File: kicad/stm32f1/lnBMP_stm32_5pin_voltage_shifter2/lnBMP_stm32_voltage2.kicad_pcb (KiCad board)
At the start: 2 copper layers, 52.6 x 33 mm, 1 part, among them J1 Debug port

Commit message: beginning GD32 version
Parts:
- added C16: 100n, Resistor_SMD:R_0603_1608Metric, F.Cu at (167.3, 68.5)
- added C17: 100n, Resistor_SMD:R_0603_1608Metric, F.Cu at (122.3, 104.0)
- added C18: 100n, Resistor_SMD:R_0603_1608Metric, F.Cu at (122.3, 106.5)
- added C19: 100n, Resistor_SMD:R_0603_1608Metric, F.Cu at (122.3, 109.0)
- added C20: 100n, Resistor_SMD:R_0603_1608Metric, F.Cu at (122.3, 111.5)
- added C22: 100n, Resistor_SMD:R_0603_1608Metric, F.Cu at (134.2, 107.3)
- added C24: 100n, Resistor_SMD:R_0603_1608Metric, F.Cu at (134.2, 109.8)
- added C3: 100n, Resistor_SMD:R_0603_1608Metric, F.Cu at (166.0, 74.5)
- added C4: 100n, Resistor_SMD:R_0603_1608Metric, F.Cu at (112.5, 58.2)
- added C5: 100u, Capacitor_SMD:C_1206_3216Metric_Pad1.33x1.80mm_HandSolder, F.Cu at (148.2, 81.0)
- added C6: 100n, Resistor_SMD:R_0603_1608Metric, F.Cu at (148.8, 83.7)
- added C7: 22pf, Resistor_SMD:R_0603_1608Metric, F.Cu at (118.6, 89.8)
- added C8: 22pf, Resistor_SMD:R_0603_1608Metric, F.Cu at (118.6, 93.4)
- added D1: LED, Diode_SMD:D_0805_2012Metric, F.Cu at (143.0, 98.6)
- added D2: LED, Diode_SMD:D_0805_2012Metric, F.Cu at (152.6, 83.3)
- added J2: Debug port, Connector_JST:JST_XH_B5B-XH-AM_1x05_P2.50mm_Vertical, F.Cu at (139.8, 82.5)
- added J3: USB, Connector_USB:USB_C_Receptacle_Palconn_UTC16-G, F.Cu at (150.6, 91.7)
- added J4: DFU, Connector_PinHeader_1.27mm:PinHeader_1x02_P1.27mm_Vertical, F.Cu at (132.2, 57.0)
- added J5: BOOT, Connector_PinHeader_1.27mm:PinHeader_1x02_P1.27mm_Vertical, F.Cu at (136.4, 57.0)
- added J6: jtag, Connector_PinHeader_1.27mm:PinHeader_2x05_P1.27mm_Vertical_SMD, F.Cu at (108.0, 94.3)
- added J9: Conn_01x03_Socket, Connector_PinHeader_1.27mm:PinHeader_1x03_P1.27mm_Vertical, F.Cu at (117.1, 65.4)
- added R1: 10k, Resistor_SMD:R_0603_1608Metric, F.Cu at (141.0, 57.2)
- added R10: 330, Resistor_SMD:R_0603_1608Metric, F.Cu at (152.5, 80.9)
- added R2: 330, Resistor_SMD:R_0603_1608Metric, F.Cu at (142.7, 96.4)
- added R3: 10k, Resistor_SMD:R_0603_1608Metric, F.Cu at (145.0, 58.8)
- added R4: 1k, Resistor_SMD:R_0603_1608Metric, F.Cu at (170.0, 77.0)
- added R5: 22, Resistor_SMD:R_0603_1608Metric, F.Cu at (142.8, 92.7)
- added R6: 22, Resistor_SMD:R_0603_1608Metric, F.Cu at (142.8, 91.1)
- added R7: 1.2k, Resistor_SMD:R_0603_1608Metric, F.Cu at (142.8, 89.5)
- added R8: 5.1k, Resistor_SMD:R_0603_1608Metric, F.Cu at (145.7, 89.0)
- added R9: 5.1k, Resistor_SMD:R_0603_1608Metric, F.Cu at (145.7, 93.9)
- added RST1: SW2, Button_Switch_SMD:SW_SPST_CK_RS282G05A3, F.Cu at (135.6, 52.8)
- added U1: GD32F303, Package_QFP:LQFP-48_7x7mm_P0.5mm, F.Cu at (130.2, 91.4)
- added U2: 3V->VTREF, Package_SO:VSSOP-8_2.3x2mm_P0.5mm, F.Cu at (102.2, 60.5)
- added U3: VTREF->3V, Package_SO:VSSOP-8_2.3x2mm_P0.5mm, F.Cu at (102.1, 49.4)
- added U4: VTREF<->3V, Package_SO:VSSOP-8_2.3x2mm_P0.5mm, F.Cu at (102.1, 55.0)
- added U5: LM1117-3.3, Package_TO_SOT_SMD:SOT-223, F.Cu at (149.3, 74.2)
- added U8: RT9013-33GB, PCM_Package_TO_SOT_SMD_AKL:TSOT-23-5, F.Cu at (102.1, 43.1)
- added Y2: 8Mhz, Crystal:Crystal_SMD_TXC_7M-4Pin_3.2x2.5mm, F.Cu at (121.8, 91.5)
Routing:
- net +3.3V: track 0.00 -> 37.8 mm, vias 0 -> 3
- net GND: track 0.00 -> 37.5 mm
- net Net-(U5-VI): track 0.00 -> 26.4 mm, vias 0 -> 3
- net Net-(U1-PD0): track 0.00 -> 10.4 mm
- net DP: track 0.00 -> 10.1 mm
- net Net-(U1-PD1): track 0.00 -> 9.16 mm
- net Net-(U1-PB13): track 0.00 -> 8.61 mm
- net DN: track 0.00 -> 8.37 mm
- net D-: track 0.00 -> 7.67 mm
- net D+: track 0.00 -> 6.22 mm
- net Net-(J3-CC2): track 0.00 -> 2.42 mm
- net Net-(J3-CC1): track 0.00 -> 2.40 mm
- net Net-(D2-A): track 0.00 -> 1.95 mm
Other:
- board size 52.6 x 33 mm -> 52.6 x 31.7 mm

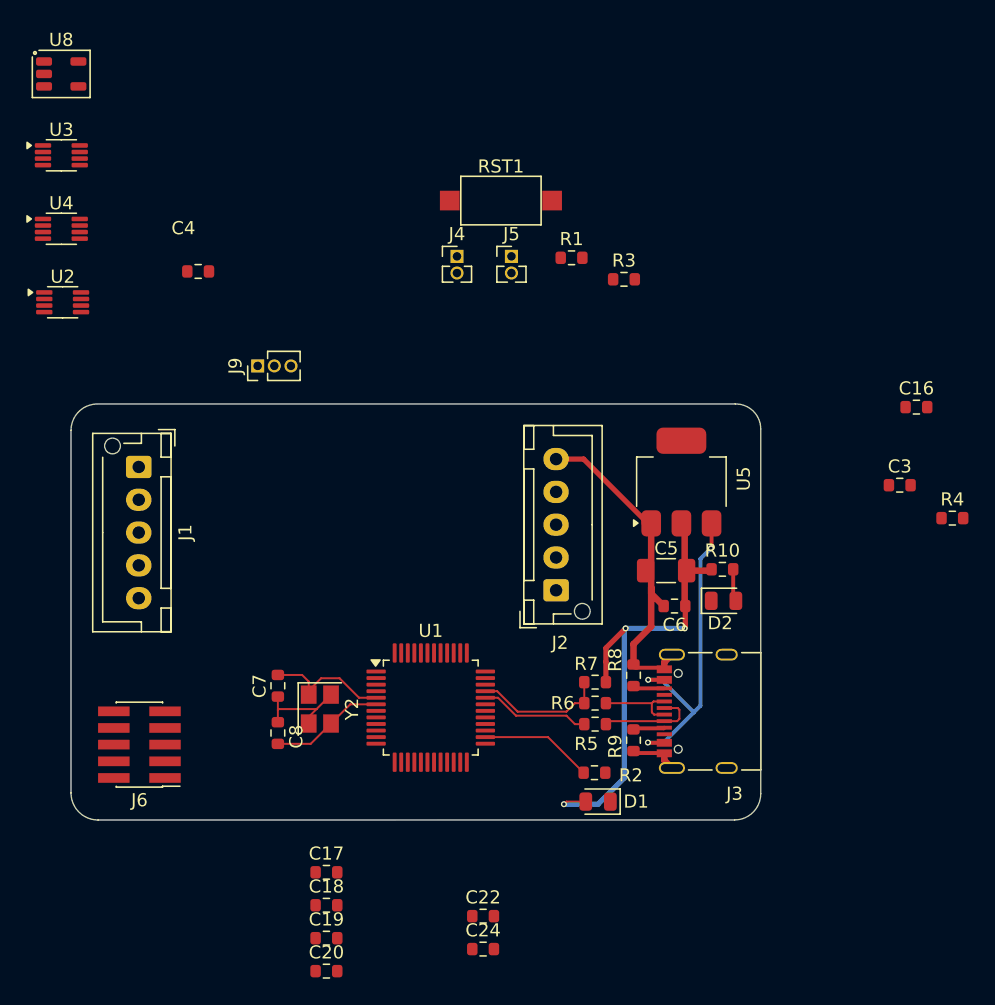
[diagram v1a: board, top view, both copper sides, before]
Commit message: first run at gd32 pcb with voltage shifter
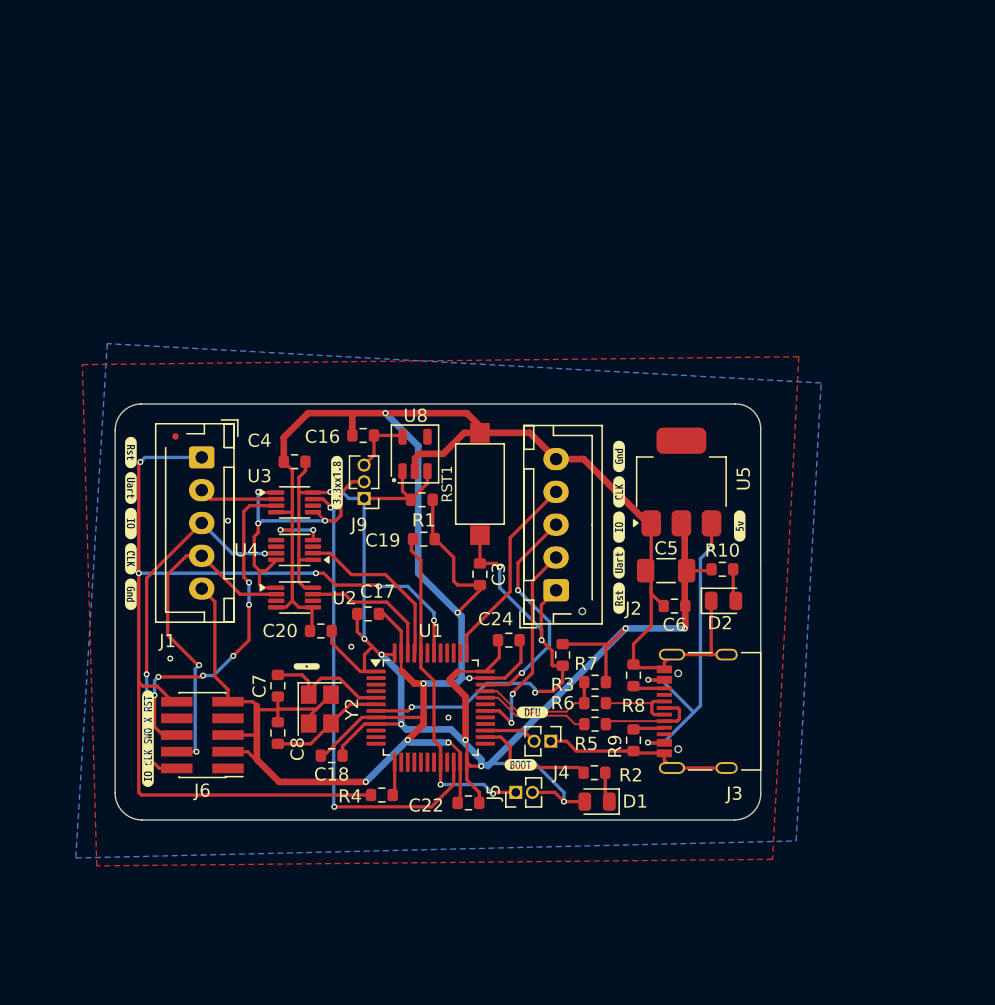
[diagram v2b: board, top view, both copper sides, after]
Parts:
- added kibuzzard-672226BD: G***, kibuzzard-672226BD, F.Cu at (120.8, 88.3)
- added kibuzzard-672281C9: G***, kibuzzard-672281C9, F.Cu at (144.6, 77.7)
- added kibuzzard-672281C9: G***, kibuzzard-672281C9, F.Cu at (107.4, 77.4)
- added kibuzzard-672281D4: G***, kibuzzard-672281D4, F.Cu at (107.4, 80.1)
- added kibuzzard-672281D4: G***, kibuzzard-672281D4, F.Cu at (144.6, 75.0)
- added kibuzzard-672281DC: G***, kibuzzard-672281DC, F.Cu at (144.6, 80.4)
- added kibuzzard-672281DC: G***, kibuzzard-672281DC, F.Cu at (107.4, 74.7)
- added kibuzzard-672281E9: G***, kibuzzard-672281E9, F.Cu at (107.4, 72.0)
- added kibuzzard-672281E9: G***, kibuzzard-672281E9, F.Cu at (144.6, 83.1)
- added kibuzzard-6722820B: G***, kibuzzard-6722820B, F.Cu at (107.4, 82.8)
- added kibuzzard-6722820B: G***, kibuzzard-6722820B, F.Cu at (144.6, 72.3)
- added kibuzzard-67228234: G***, kibuzzard-67228234, F.Cu at (153.8, 77.6)
- added kibuzzard-672282C7: G***, kibuzzard-672282C7, F.Cu at (108.7, 93.8)
- added kibuzzard-67228302: G***, kibuzzard-67228302, F.Cu at (137.1, 95.8)
- added kibuzzard-6722831C: G***, kibuzzard-6722831C, F.Cu at (138.0, 91.8)
- added kibuzzard-672283BF: G***, kibuzzard-672283BF, F.Cu at (123.1, 74.3)
- moved R4 48.3 mm to (126.5, 98.1)
- moved C16 42.2 mm to (125.1, 70.7), turned to 180 degrees
- moved J5 40.9 mm to (136.7, 97.9), turned to 90 degrees
- moved U8 39.6 mm to (129.1, 72.1), turned to 90 degrees
- moved J4 37.6 mm to (139.4, 94.0), turned to -90 degrees
- moved C19 34.2 mm to (129.6, 75.6)
- moved C3 32.7 mm to (134.0, 81.3), turned to -90 degrees
- moved U3 31.9 mm to (119.9, 75.8)
- moved U4 30.2 mm to (119.9, 79.4), turned to 180 degrees
- moved R3 29.0 mm to (140.3, 87.4), turned to -90 degrees
- moved U2 28.6 mm to (119.9, 83.0)
- moved C20 25.9 mm to (121.9, 85.6), turned to 180 degrees
- moved R1 24.2 mm to (129.7, 78.6)
- moved C24 23.6 mm to (136.2, 86.3)
- moved RST1 21.7 mm to (134.0, 74.4), turned to 90 degrees
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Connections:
- C17 pad 2: Net-(C17-Pad2) -> GND
- C18 pad 2: Net-(C17-Pad2) -> GND
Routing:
- net GND: track 37.5 -> 217.8 mm, vias 0 -> 13
- net +3.3V: track 37.8 -> 136.9 mm, vias 3 -> 9
- net INOUT_NRESET: track 0.00 -> 77.9 mm, vias 0 -> 5
- net OUT_UART_RX_3V: track 0.00 -> 36.1 mm, vias 0 -> 2
- net NRST: track 0.00 -> 35.1 mm, vias 0 -> 4
- net OUT_SWDIO: track 0.00 -> 28.2 mm, vias 0 -> 3
- net OUT_SWDCLK: track 0.00 -> 26.1 mm, vias 0 -> 2
- net INOUT_SWO: track 0.00 -> 25.6 mm, vias 0 -> 6
- net Net-(J5-Pin_1): track 0.00 -> 25.5 mm, vias 0 -> 2
- net VTREF: track 0.00 -> 23.1 mm, vias 0 -> 3
- net SWDIO: track 0.00 -> 17.5 mm, vias 0 -> 2
- net UART_TX: track 0.00 -> 16.3 mm, vias 0 -> 2
- net SWDCLK: track 0.00 -> 15.1 mm
- net OUT_SWDIO_3V: track 0.00 -> 13.1 mm
- net OUT_SWDCLK_3V: track 0.00 -> 10.4 mm
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- added copper zone on B.Cu, net GND
- added copper zone on F.Cu, net GND
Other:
- board size 52.6 x 31.7 mm -> 49.2 x 31.7 mm
